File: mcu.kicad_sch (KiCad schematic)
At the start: 8 parts, among them J1 USB4105-GF-A, U1 ESP32-C6-MINI-1, U4 FT231XQ

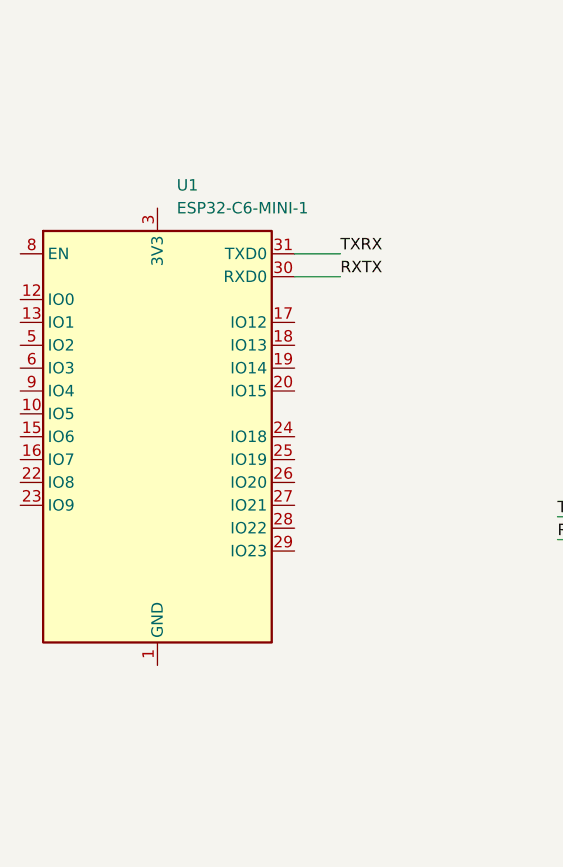
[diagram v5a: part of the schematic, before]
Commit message: added 3v3 line to ESP
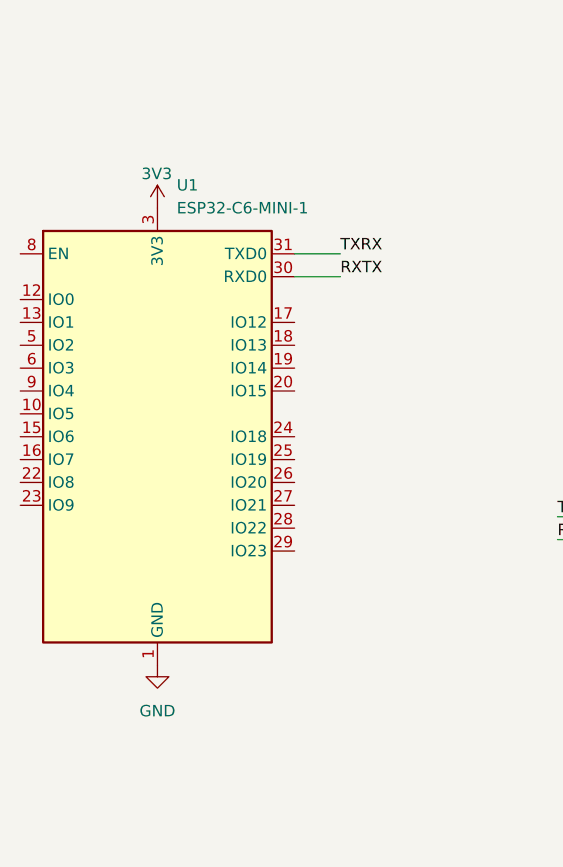
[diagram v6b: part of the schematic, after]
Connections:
- net 3V3: now also U1.3 (3V3)
- net GND: now also U1.1 (GND), U1.11 (GND), U1.14 (GND), U1.2 (GND), U1.36 (GND), U1.37 (GND), U1.38 (GND), U1.39 (GND), U1.40 (GND), U1.41 (GND), U1.42 (GND), U1.43 (GND), U1.44 (GND), U1.45 (GND), U1.46 (GND), U1.47 (GND), U1.48 (GND), U1.49 (GND), U1.50 (GND), U1.51 (GND), U1.52 (GND), U1.53 (GND)
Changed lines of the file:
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@@
+	(symbol
+		(lib_id "power:GND")
+		(at 137.16 118.11 0)
+		(unit 1)
+		(exclude_from_sim no)
+		(in_bom yes)
+		(on_board yes)
+		(dnp no)
+		(fields_autoplaced yes)
+		(property "Reference" "#PWR038"
+			(at 137.16 124.46 0)
+			(effects
+				(font
+					(size 1.27 1.27)
+				)
+				(hide yes)
+			)
+		)
+		(property "Value" "GND"
+			(at 137.16 123.19 0)
+			(effects
+				(font
+					(size 1.27 1.27)
+				)
+			)
+		)
+		(property "Footprint" ""
+			(at 137.16 118.11 0)
+			(effects
+				(font
+					(size 1.27 1.27)
+				)
+				(hide yes)
+			)
+		)
+		(property "Datasheet" ""
+			(at 137.16 118.11 0)
+			(effects
+				(font
+					(size 1.27 1.27)
+				)
+				(hide yes)
+			)
+		)
+		(property "Description" "Power symbol creates a global label with name \"GND\" , ground"
+			(at 137.16 118.11 0)
+			(effects
+				(font
+					(size 1.27 1.27)
+				)
+				(hide yes)
+			)
+		)
+		(pin "1"
+		)
+		(instances
+			(project "PALReceiver"
+				(path "/2785bbdd-da8c-4c23-b498-605d17251f95/329eb62d-f8d8-4a30-9cb6-995f07524828"
+					(reference "#PWR038")
+					(unit 1)
+				)
+			)
+		)
+	)
+	(symbol
+		(lib_id "power:+1V0")
+		(at 137.16 67.31 0)
+		(unit 1)
+		(exclude_from_sim no)
+		(in_bom yes)
+		(on_board yes)
+		(dnp no)
+		(property "Reference" "#PWR039"
+			(at 137.16 71.12 0)
+			(effects
+				(font
+					(size 1.27 1.27)
+				)
+				(hide yes)
+			)
+		)
+		(property "Value" "3V3"
+			(at 135.382 63.5 0)
+			(effects
+				(font
+					(size 1.27 1.27)
+				)
+				(justify left)
+			)
+		)
+		(property "Footprint" ""
+			(at 137.16 67.31 0)
+			(effects
+				(font
+					(size 1.27 1.27)
+				)
+				(hide yes)
+			)
+		)
+		(property "Datasheet" ""
+			(at 137.16 67.31 0)
+			(effects
+				(font
+					(size 1.27 1.27)
+				)
+				(hide yes)
+			)
+		)
+		(property "Description" "Power symbol creates a global label with name \"+1V0\""
+			(at 137.16 67.31 0)
+			(effects
+				(font
+					(size 1.27 1.27)
+				)
+				(hide yes)
+			)
+		)
+		(pin "1"
+		)
+		(instances
+			(project "PALReceiver"
+				(path "/2785bbdd-da8c-4c23-b498-605d17251f95/329eb62d-f8d8-4a30-9cb6-995f07524828"
+					(reference "#PWR039")
+					(unit 1)
+				)
+			)
+		)
+	)
 	(symbol
 		(lib_id "power:GND")

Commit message: added transistor
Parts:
- added Q2: BC847BDW1, Package_TO_SOT_SMD:SOT-363_SC-70-6, symbol Transistor_BJT:BC847BDW1
- added R10, R11: 10k, symbol Device:R_US
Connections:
- net GND: now also Q2.5 (B2), R11.2
- net C31: now reaches C31.2, U4.10 (3V3OUT), U4.11 (~{RESET}), U4.20 (VCCIO)
- net DTR: now reaches U4.18 (~{DTR})
- net DTR: now also Q2.1 (E1), R11.1
- net RTS: now reaches U4.19 (~{RTS})
- net RTS: now also Q2.4 (E2), R10.1
- new net: Q2.2 (B1), R10.2
- new net CHIP_PU: Q2.3 (C2)
- new net IO9: Q2.6 (C1)
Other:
- moved on the sheet: C31
